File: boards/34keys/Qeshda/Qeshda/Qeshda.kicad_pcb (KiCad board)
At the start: 2 copper layers, 230.5 x 102.4 mm, 84 parts, among them J1 Conn_01x08_Female, SW1 SW_Push, SW10 SW_Push, SW11 SW_Push, SW12 SW_Push, SW13 SW_Push, SW14 SW_Push, SW15 SW_Push, SW16 SW_Push, SW17 SW_Push, SW18 SW_Push, SW19 SW_Push, SW2 SW_Push, SW20 SW_Push, SW21 SW_Push, SW22 SW_Push, SW23 SW_Push, SW24 SW_Push, SW25 SW_SPDT, SW26 Rotary_Encoder_Switch, SW27 SW_Push, SW28 SW_Push, SW29 SW_Push, SW3 SW_Push, SW30 SW_Push, SW31 SW_Push, SW32 SW_Push, SW33 SW_SPDT, SW34 SW_Push, SW37 SW_Push, SW38 SW_Push, SW39 SW_Push, SW4 SW_Push, SW40 SW_Push, SW5 SW_Push, SW6 SW_Push, SW7 SW_Push, SW8 SW_Push, SW9 SW_Push, U1 nice_nano

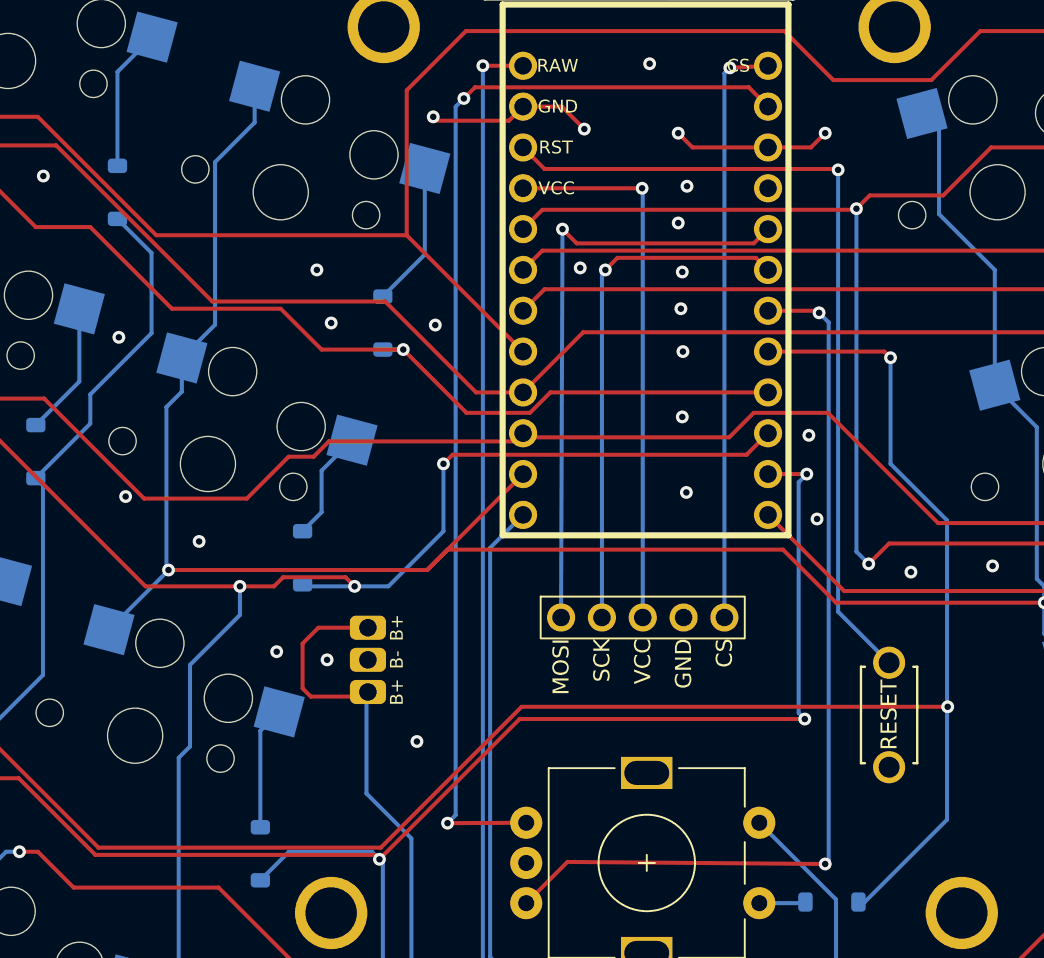
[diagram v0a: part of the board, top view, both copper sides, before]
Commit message: Qeshda: JST connector angled
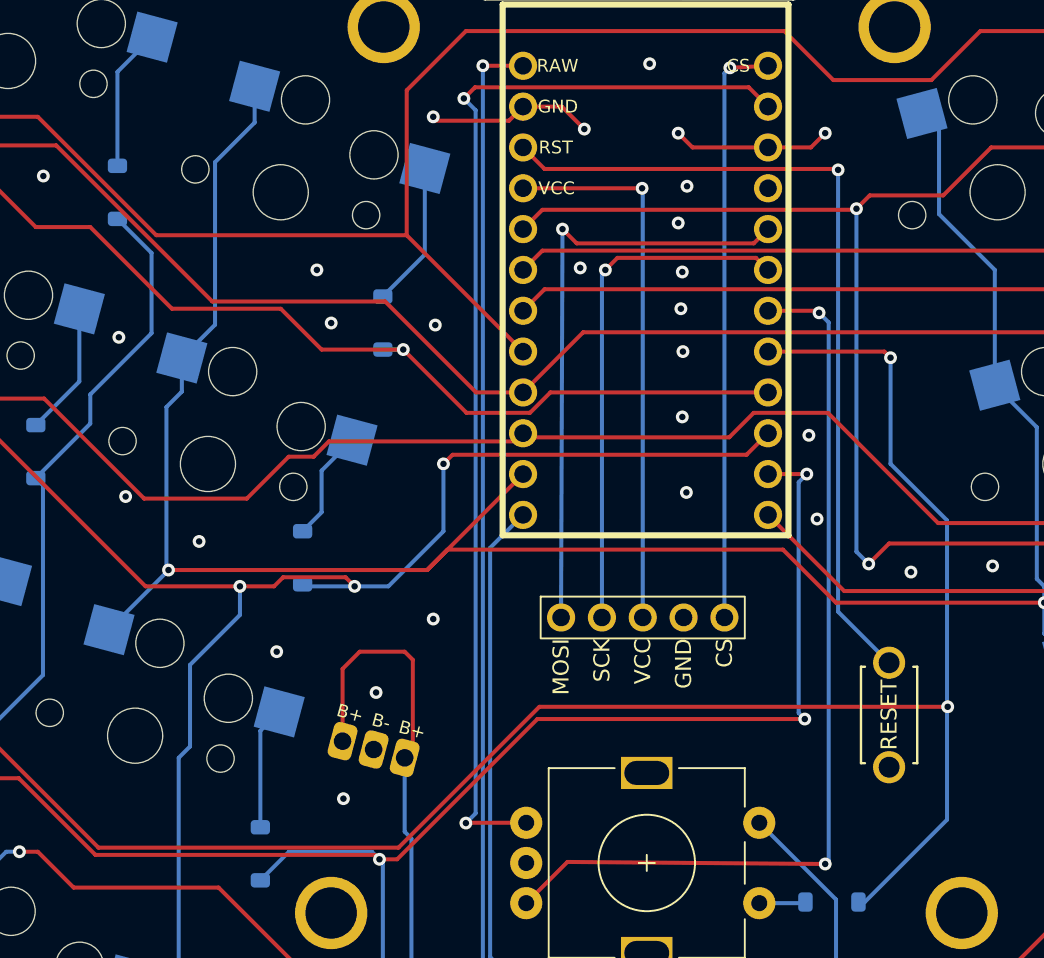
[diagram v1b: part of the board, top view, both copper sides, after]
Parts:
- moved J1 5.59 mm to (137.0, 92.2), turned to 165 degrees
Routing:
- net EncL: track 70.1 -> 69.1 mm
- net bat+: track 54.4 -> 53.5 mm
- net GND: vias 46 -> 47
